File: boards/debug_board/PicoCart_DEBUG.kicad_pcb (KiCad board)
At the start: 2 copper layers, 97.5 x 95.6 mm, 27 parts, among them J1 D_DEBUG, J2 Micro_SD_Card, J3 UART, J4 DEBUG, J5 MSX Debug, J6 D_UART, J7 Ground Pins, J8 Ground Pins, J9 DEBUG_I2C, U1 LD1117S33TR_SOT223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

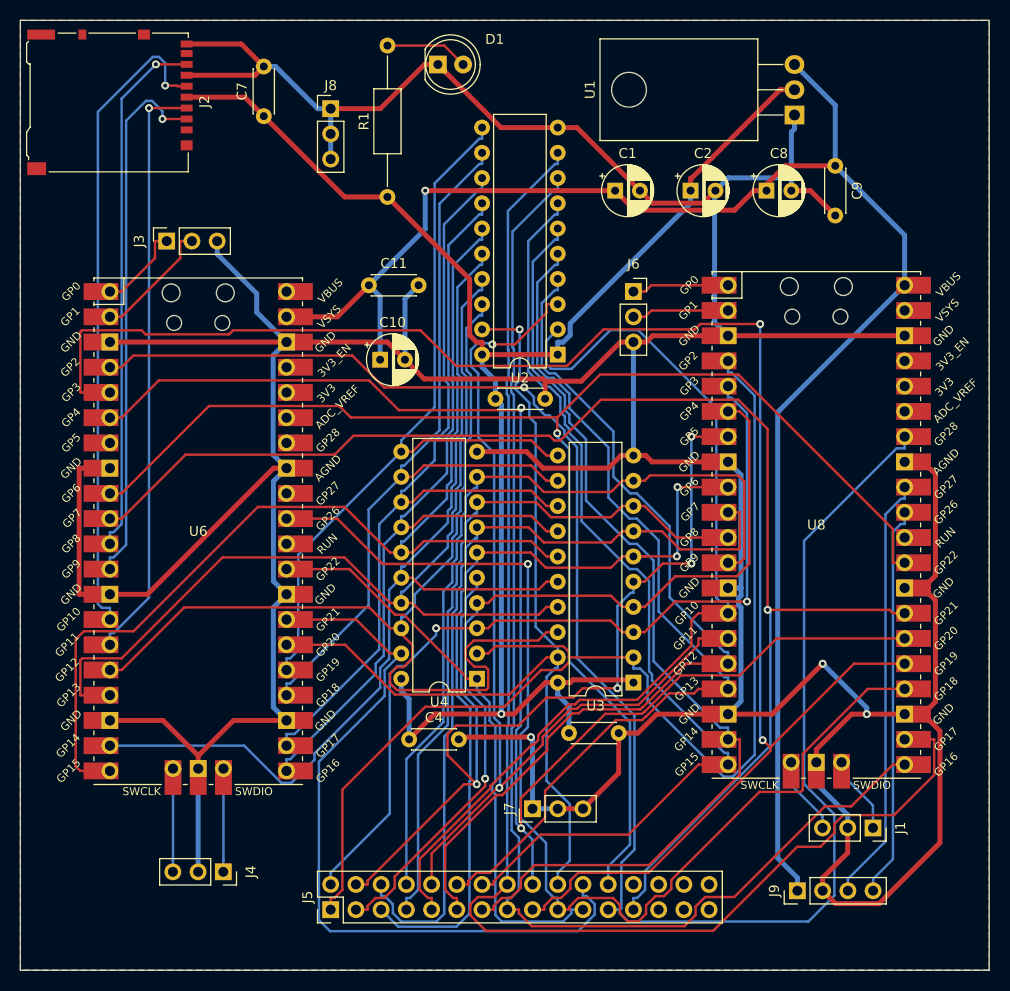
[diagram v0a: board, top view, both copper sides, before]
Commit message: Fixed circuit - last design would not have worked
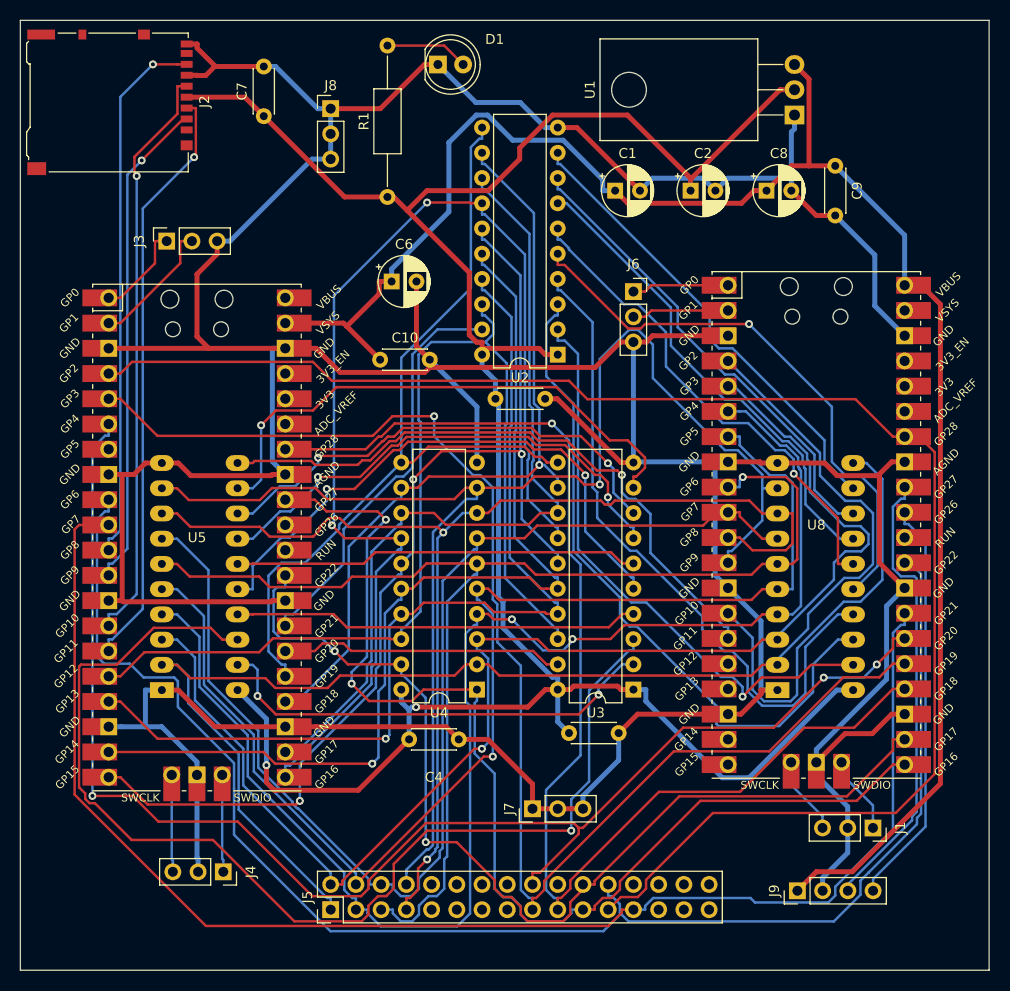
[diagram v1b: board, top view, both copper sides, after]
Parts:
- removed C11: 100nF, Capacitor_THT:C_Disc_D4.3mm_W1.9mm_P5.00mm
- added C6: 1uF, Capacitor_THT:CP_Radial_D5.0mm_P2.50mm, F.Cu at (86.8, 59.3)
- added U5: Pico, PicoCartLibrary:RPi_Pico_SMD_TH, F.Cu at (67.2, 85.1)
- added U7: 74HCT574, Package_DIP:DIP-20_W7.62mm_Socket_LongPads, B.Cu at (63.6, 100.4)
- C10: value 1uF -> 100nF; footprint Capacitor_THT:CP_Radial_D5.0mm_P2.50mm -> Capacitor_THT:C_Disc_D4.3mm_W1.9mm_P5.00mm
- U6: value Pico -> 74HCT574; footprint PicoCartLibrary:RPi_Pico_SMD_TH -> Package_DIP:DIP-20_W7.62mm_Socket_LongPads; moved to B.Cu
- moved U6 60.5 mm to (125.6, 100.4)
- moved U4 1.10 mm to (95.4, 100.4)
- moved U3 0.70 mm to (111.1, 100.4)
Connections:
- U2 pad 19: /AOE -> /ALOE
- U2 pad 2: /E_A8 -> /A0
- U2 pad 3: /E_A9 -> /A1
- U2 pad 4: /E_A10 -> /A2
- U2 pad 5: /E_A11 -> /A3
- U2 pad 6: /E_A12 -> /A4
- U2 pad 7: /E_A13 -> /A5
- U2 pad 8: /E_A14 -> /A6
- U2 pad 9: /E_A15 -> /A7
- U3 pad 19: /AOE -> /AHOE
- U3 pad 2: /E_A0 -> /A8
- U3 pad 3: /E_A1 -> /A9
- U3 pad 4: /E_A2 -> /A10
- U3 pad 5: /E_A3 -> /A11
- U3 pad 6: /E_A4 -> /A12
- U3 pad 7: /E_A5 -> /A13
- U3 pad 8: /E_A6 -> /A14
- U3 pad 9: /E_A7 -> /A15
- U6 pad 1: UART_TX -> GND
- U6 pad 10: /I_WRITE -> GND
- U6 pad 11: SPI_MISO -> AL_PULSE
- U6 pad 12: SPI_CS -> /A7
- U6 pad 13: GND -> /A6
- U6 pad 14: SPI_SCK -> /A5
- U6 pad 15: SPI_MOSI -> /A4
- U6 pad 16: /I_D0 -> /A3
- U6 pad 17: /I_D1 -> /A2
- U6 pad 18: GND -> /A1
- U6 pad 19: /I_D2 -> /A0
- U6 pad 2: UART_RX -> /E_A0
- U6 pad 20: /I_D3 -> +3.3V
- U6 pad 3: GND -> /E_A1
- U6 pad 4: /I_SLTSEL -> /E_A2
- U6 pad 5: /I_CS1 -> /E_A3
- U6 pad 6: /I_CS2 -> /E_A4
- U6 pad 7: unconnected-(U6-GPIO5-Pad7) -> /E_A5
- U6 pad 8: GND -> /E_A6
- U6 pad 9: /I_READ -> /E_A7
- U8 pad 14: /E_A8 -> AL_PULSE
- U8 pad 15: /E_A9 -> AH_PULSE
- U8 pad 16: /E_A10 -> unconnected-(U8-GPIO12-Pad16)_0
- U8 pad 17: /E_A11 -> unconnected-(U8-GPIO13-Pad17)_0
- U8 pad 19: /E_A12 -> unconnected-(U8-GPIO14-Pad19)_0
- U8 pad 20: /E_A13 -> unconnected-(U8-GPIO15-Pad20)
- U8 pad 21: /E_A14 -> /DOUT
- U8 pad 22: /E_A15 -> /DOE
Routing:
- net /E_A15: track 142.7 -> 0.00 mm
- net /E_A14: track 125.2 -> 0.00 mm
- net /A9: track 0.00 -> 113.6 mm, vias 0 -> 1
- net /E_A9: track 99.4 -> 0.00 mm, vias 2 -> 0
- net /E_A12: track 99.1 -> 0.00 mm
- net /E_A13: track 97.2 -> 0.00 mm
- net /E_A8: track 96.8 -> 0.00 mm
- net /AOE: track 94.8 -> 0.00 mm, vias 1 -> 0
- net /E_A10: track 92.2 -> 0.00 mm
- net /E_A11: track 91.1 -> 0.00 mm
- net /A1: track 0.00 -> 69.5 mm
- net +3.3V: track 164.1 -> 232.5 mm, vias 1 -> 2
- net /A2: track 0.00 -> 68.3 mm
- net AH_PULSE: track 0.00 -> 63.6 mm, vias 0 -> 1
- net /A0: track 0.00 -> 59.1 mm, vias 0 -> 1
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- removed copper zone on B.Cu, net GND
- removed copper zone on F.Cu, net GND

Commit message: Add Test Points for Spare GPIO Pins
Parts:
- added G***: LOGO, LOGO, B.Cu at (98.2, 80.8)
- added TP1: TestPoint, TestPoint:TestPoint_Pad_D1.0mm, F.Cu at (113.4, 97.7)
- added TP2: TestPoint, TestPoint:TestPoint_Pad_D1.0mm, F.Cu at (113.8, 100.5)
- added TP3: TestPoint, TestPoint:TestPoint_Pad_D1.0mm, F.Cu at (113.5, 105.7)
- added TP4: TestPoint, TestPoint:TestPoint_Pad_D1.0mm, F.Cu at (114.2, 109.4)
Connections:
- U8 pad 16: unconnected-(U8-GPIO12-Pad16)_0 -> Net-(U8-GPIO12)
- U8 pad 17: unconnected-(U8-GPIO13-Pad17)_0 -> Net-(U8-GPIO13)
- U8 pad 19: unconnected-(U8-GPIO14-Pad19)_0 -> Net-(U8-GPIO14)
- U8 pad 20: unconnected-(U8-GPIO15-Pad20) -> Net-(U8-GPIO15)
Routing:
- net Net-(U8-GPIO12): track 0.00 -> 7.26 mm
- net Net-(U8-GPIO14): track 0.00 -> 7.24 mm
- net Net-(U8-GPIO15): track 0.00 -> 7.02 mm
- net Net-(U8-GPIO13): track 0.00 -> 6.89 mm
- net /I_CS2: track 144.6 -> 146.4 mm
- added copper zone on B.Cu, net GND
- added copper zone on F.Cu, net GND
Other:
- outline, holes or cut-outs redrawn
- board text added: "PicoCart Debug Rev 1b 2024/03/08 - Yassir Al-Refaie"
